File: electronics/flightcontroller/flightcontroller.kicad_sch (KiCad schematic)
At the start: 12 parts, among them J11 Payload, J13 Conn_01x04, J2 ESC+, J3 ESC, J4 Servo3, J5 Servo2, J6 Servo1, J7 ESC-

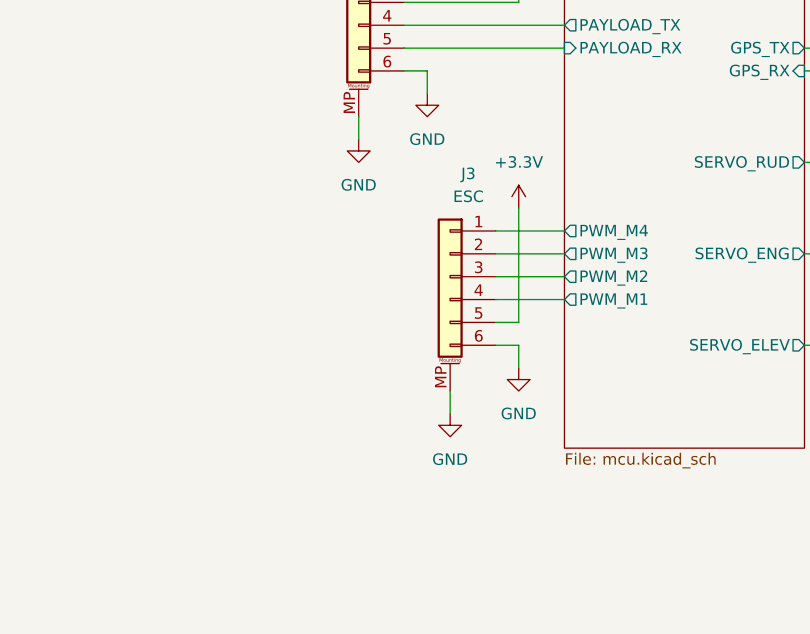
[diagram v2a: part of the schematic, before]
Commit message: electronics: Add a resistor for ESC power and some test pads.
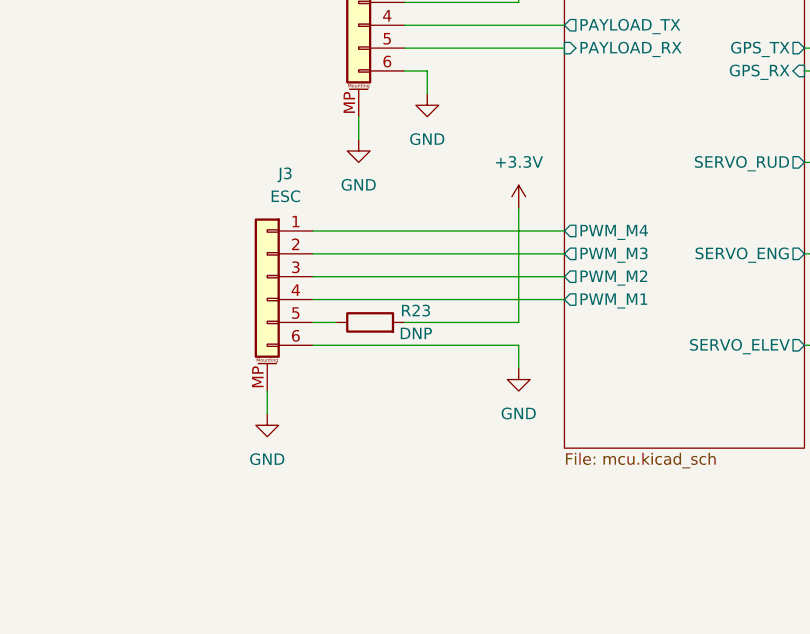
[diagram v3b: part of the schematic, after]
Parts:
- added R23: DNP, Resistor_SMD:R_0402_1005Metric, symbol Device:R
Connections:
- net +3V3: now also R23.2; no longer J3.5 (Pin_5)
- new net: J3.5 (Pin_5), R23.1
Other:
- moved on the sheet: J3
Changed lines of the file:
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@@
+    (stroke (width 0) (type solid) (color 0 0 0 0))
+  )
+  (wire (pts (xy 129.54 91.44) (xy 129.54 93.98))
+    (stroke (width 0) (type solid) (color 0 0 0 0))
+  )
+  (wire (pts (xy 134.62 73.66) (xy 162.56 73.66))
+    (stroke (width 0) (type solid) (color 0 0 0 0))
+  )
+  (wire (pts (xy 134.62 76.2) (xy 162.56 76.2))
+    (stroke (width 0) (type solid) (color 0 0 0 0))
+  )
+  (wire (pts (xy 134.62 78.74) (xy 162.56 78.74))
+    (stroke (width 0) (type solid) (color 0 0 0 0))
+  )
+  (wire (pts (xy 134.62 81.28) (xy 162.56 81.28))
+    (stroke (width 0) (type solid) (color 0 0 0 0))
+  )
+  (wire (pts (xy 137.16 83.82) (xy 134.62 83.82))
     (stroke (width 0) (type solid) (color 0 0 0 0))
   )
@@
     (stroke (width 0) (type solid) (color 0 0 0 0))
   )
-  (wire (pts (xy 149.86 91.44) (xy 149.86 93.98))
-    (stroke (width 0) (type solid) (color 0 0 0 0))
-  )
   (wire (pts (xy 152.4 45.72) (xy 152.4 40.64))
     (stroke (width 0) (type solid) (color 0 0 0 0))
   )
-  (wire (pts (xy 154.94 73.66) (xy 162.56 73.66))
-    (stroke (width 0) (type solid) (color 0 0 0 0))
-  )
-  (wire (pts (xy 154.94 76.2) (xy 162.56 76.2))
-    (stroke (width 0) (type solid) (color 0 0 0 0))
-  )
-  (wire (pts (xy 154.94 78.74) (xy 162.56 78.74))
-    (stroke (width 0) (type solid) (color 0 0 0 0))
-  )
-  (wire (pts (xy 154.94 81.28) (xy 162.56 81.28))
-    (stroke (width 0) (type solid) (color 0 0 0 0))
-  )
   (wire (pts (xy 157.48 22.86) (xy 162.56 22.86))
     (stroke (width 0) (type solid) (color 0 0 0 0))
@@
     (stroke (width 0) (type solid) (color 0 0 0 0))
   )
-  (wire (pts (xy 157.48 83.82) (xy 154.94 83.82))
-    (stroke (width 0) (type solid) (color 0 0 0 0))
-  )
-  (wire (pts (xy 157.48 86.36) (xy 154.94 86.36))
+  (wire (pts (xy 157.48 83.82) (xy 144.78 83.82))
+    (stroke (width 0) (type solid) (color 0 0 0 0))
+  )
+  (wire (pts (xy 157.48 86.36) (xy 134.62 86.36))
     (stroke (width 0) (type solid) (color 0 0 0 0))
   )
@@
     (pin "1")
   )
+  (symbol (lib_id "power:GND") (at 129.54 93.98 0) (unit 1)
+    (in_bom yes) (on_board yes) (fields_autoplaced)
+    (property "Reference" "#PWR0153" (id 0) (at 129.54 100.33 0)
+      (effects (font (size 1.27 1.27)) hide)
+    )
+    (property "Value" "GND" (id 1) (at 129.54 99.06 0))
+    (property "Footprint" "" (id 2) (at 129.54 93.98 0)
+      (effects (font (size 1.27 1.27)) hide)
+    )
+    (property "Datasheet" "" (id 3) (at 129.54 93.98 0)
+      (effects (font (size 1.27 1.27)) hide)
+    )
+    (pin "1")
+  )
   (symbol (lib_id "power:GND") (at 139.7 63.5 0) (unit 1)
     (in_bom yes) (on_board yes) (fields_autoplaced)
@@
     (pin "1")
   )
-  (symbol (lib_id "power:GND") (at 149.86 93.98 0) (unit 1)
-    (in_bom yes) (on_board yes) (fields_autoplaced)
-    (property "Reference" "#PWR0153" (id 0) (at 149.86 100.33 0)
-      (effects (font (size 1.27 1.27)) hide)
-    )
-    (property "Value" "GND" (id 1) (at 149.86 99.06 0))
-    (property "Footprint" "" (id 2) (at 149.86 93.98 0)
-      (effects (font (size 1.27 1.27)) hide)
-    )
-    (property "Datasheet" "" (id 3) (at 149.86 93.98 0)
-      (effects (font (size 1.27 1.27)) hide)
-    )
-    (pin "1")
-  )
   (symbol (lib_id "power:GND") (at 157.48 88.9 0) (unit 1)
     (in_bom yes) (on_board yes) (fields_autoplaced)
@@
       (effects (font (size 1.27 1.27)) hide)
     )
+  )
+  (symbol (lib_id "Device:R") (at 140.97 83.82 90) (unit 1)
+    (in_bom yes) (on_board yes)
+    (property "Reference" "R23" (id 0) (at 146.05 82.55 90))
+    (property "Value" "DNP" (id 1) (at 146.05 85.09 90))
+    (property "Footprint" "Resistor_SMD:R_0402_1005Metric" (id 2) (at 140.97 85.598 90)
+      (effects (font (size 1.27 1.27)) hide)
+    )
+    (property "Datasheet" "~" (id 3) (at 140.97 83.82 0)
+      (effects (font (size 1.27 1.27)) hide)
+    )
+    (pin "1")
+    (pin "2")
   )
   (symbol (lib_id "Connector_Generic:Conn_01x01") (at 46.99 93.98 0) (unit 1)
@@
     (pin "MP")
   )
-  (symbol (lib_id "Connector_Generic_MountingPin:Conn_01x06_MountingPin") (at 139.7 48.26 0) (mirror y) (unit 1)
-    (in_bom yes) (on_board yes) (fields_autoplaced)
-    (property "Reference" "J11" (id 0) (at 141.732 36.83 0))
-    (property "Value" "Payload" (id 1) (at 141.732 39.37 0))
-    (property "Footprint" "Connector_JST:JST_SH_SM06B-SRSS-TB_1x06-1MP_P1.00mm_Horizontal" (id 2) (at 139.7 48.26 0)
-      (effects (font (size 1.27 1.27)) hide)
-    )
-    (property "Datasheet" "~" (id 3) (at 139.7 48.26 0)
-      (effects (font (size 1.27 1.27)) hide)
-    )
-    (property "Digikey" "455-1806-1-ND" (id 4) (at 139.7 48.26 0)
-      (effects (font (size 1.27 1.27)) hide)
-    )
-    (property "Mouser" "474-PRT-10210" (id 5) (at 139.7 48.26 0)
+  (symbol (lib_id "Connector_Generic_MountingPin:Conn_01x06_MountingPin") (at 129.54 78.74 0) (mirror y) (unit 1)
+    (in_bom yes) (on_board yes) (fields_autoplaced)
+    (property "Reference" "J3" (id 0) (at 131.572 67.31 0))
+    (property "Value" "ESC" (id 1) (at 131.572 69.85 0))
+    (property "Footprint" "Connector_JST:JST_SH_SM06B-SRSS-TB_1x06-1MP_P1.00mm_Horizontal" (id 2) (at 129.54 78.74 0)
+      (effects (font (size 1.27 1.27)) hide)
+    )
+    (property "Datasheet" "~" (id 3) (at 129.54 78.74 0)
+      (effects (font (size 1.27 1.27)) hide)
+    )
+    (property "Digikey" "455-1806-1-ND" (id 4) (at 129.54 78.74 0)
+      (effects (font (size 1.27 1.27)) hide)
+    )
+    (property "Mouser" "474-PRT-10210" (id 5) (at 129.54 78.74 0)
       (effects (font (size 1.27 1.27)) hide)
     )
@@
     (pin "MP")
   )
-  (symbol (lib_id "Connector_Generic_MountingPin:Conn_01x06_MountingPin") (at 149.86 78.74 0) (mirror y) (unit 1)
-    (in_bom yes) (on_board yes) (fields_autoplaced)
-    (property "Reference" "J3" (id 0) (at 151.892 67.31 0))
-    (property "Value" "ESC" (id 1) (at 151.892 69.85 0))
-    (property "Footprint" "Connector_JST:JST_SH_SM06B-SRSS-TB_1x06-1MP_P1.00mm_Horizontal" (id 2) (at 149.86 78.74 0)
-      (effects (font (size 1.27 1.27)) hide)
-    )
-    (property "Datasheet" "~" (id 3) (at 149.86 78.74 0)
-      (effects (font (size 1.27 1.27)) hide)
-    )
-    (property "Digikey" "455-1806-1-ND" (id 4) (at 149.86 78.74 0)
-      (effects (font (size 1.27 1.27)) hide)
-    )
-    (property "Mouser" "474-PRT-10210" (id 5) (at 149.86 78.74 0)
+  (symbol (lib_id "Connector_Generic_MountingPin:Conn_01x06_MountingPin") (at 139.7 48.26 0) (mirror y) (unit 1)
+    (in_bom yes) (on_board yes) (fields_autoplaced)
+    (property "Reference" "J11" (id 0) (at 141.732 36.83 0))
+    (property "Value" "Payload" (id 1) (at 141.732 39.37 0))
+    (property "Footprint" "Connector_JST:JST_SH_SM06B-SRSS-TB_1x06-1MP_P1.00mm_Horizontal" (id 2) (at 139.7 48.26 0)
+      (effects (font (size 1.27 1.27)) hide)
+    )
+    (property "Datasheet" "~" (id 3) (at 139.7 48.26 0)
+      (effects (font (size 1.27 1.27)) hide)
+    )
+    (property "Digikey" "455-1806-1-ND" (id 4) (at 139.7 48.26 0)
+      (effects (font (size 1.27 1.27)) hide)
+    )
+    (property "Mouser" "474-PRT-10210" (id 5) (at 139.7 48.26 0)
       (effects (font (size 1.27 1.27)) hide)
     )
@@
       (reference "#PWR0157") (unit 1) (value "GND") (footprint "")
     )
+    (path "/710bac8f-b93a-494c-bd4c-06642d1701c5/8adb6a84-0fbc-4421-a085-b8899c8ee87e"
+      (reference "#PWR0158") (unit 1) (value "+3.3V") (footprint "")
+    )
     (path "/035be36c-3be5-4834-b928-6ed73ad80857/aaebbb33-6bc1-450c-a5ad-9e9ec832cc60"
       (reference "C1") (unit 1) (value "0.1uF") (footprint "Capacitor_SMD:C_0402_1005Metric")
@@
       (reference "R22") (unit 1) (value "5.1k") (footprint "Resistor_SMD:R_0402_1005Metric")
     )
+    (path "/2a5acd03-3764-40bc-b20e-6f9352c94cb8"
+      (reference "R23") (unit 1) (value "DNP") (footprint "Resistor_SMD:R_0402_1005Metric")
+    )
     (path "/9e22fcca-13c3-4897-835c-f83365def6e5/719a0b0c-6071-4ff4-af80-4a3792d2d8c0"
       (reference "SW1") (unit 1) (value "RESET") (footprint "flightcontroller-footprints:SW_SPST_PTS815")
@@
       (reference "TP1") (unit 1) (value "SWO") (footprint "TestPoint:TestPoint_Pad_D2.0mm")
     )
+    (path "/9e22fcca-13c3-4897-835c-f83365def6e5/1a3657b7-43ad-4afb-814f-713190bcb1b5"
+      (reference "TP2") (unit 1) (value "DAT1") (footprint "TestPoint:TestPoint_Pad_D2.0mm")
+    )
     (path "/035be36c-3be5-4834-b928-6ed73ad80857/f0e50344-1b2a-43a9-a48f-bb9e18ff0cfb"
